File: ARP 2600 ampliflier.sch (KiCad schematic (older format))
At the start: 39 parts, among them P1 CONN_01X04, P2 CONN_01X04, P3 CONN_01X04, P4 CONN_01X04, Q1 PN2222A, U1 TDA7269A, U2 LM7812CT, U3 LM7912CT

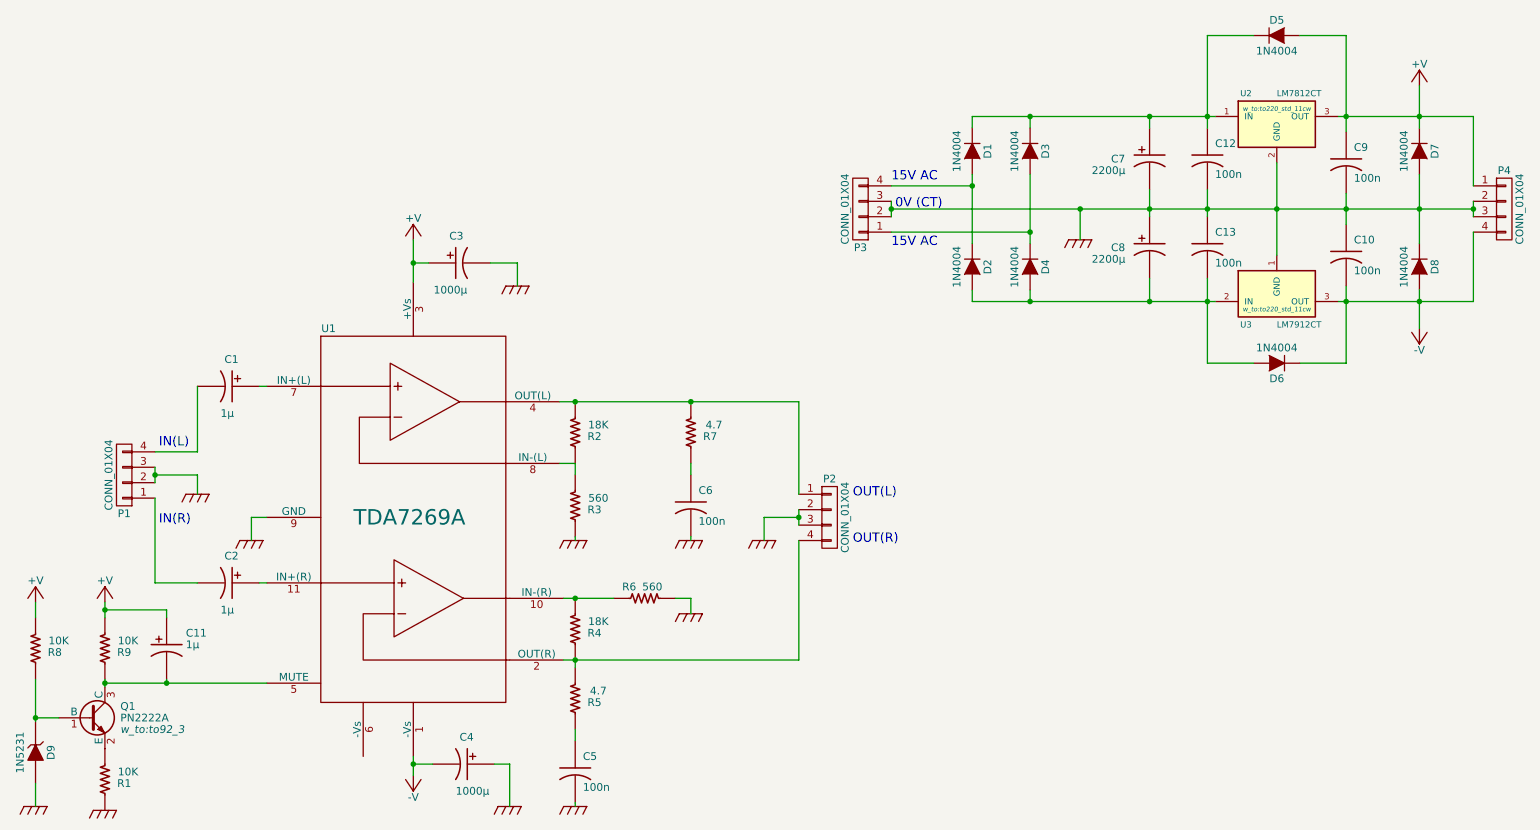
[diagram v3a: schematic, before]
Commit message: fixed pintout error with T0-220 footprints, fix Q1 footprint pintout error, add keepout zones to heatsink landing areas on top copper
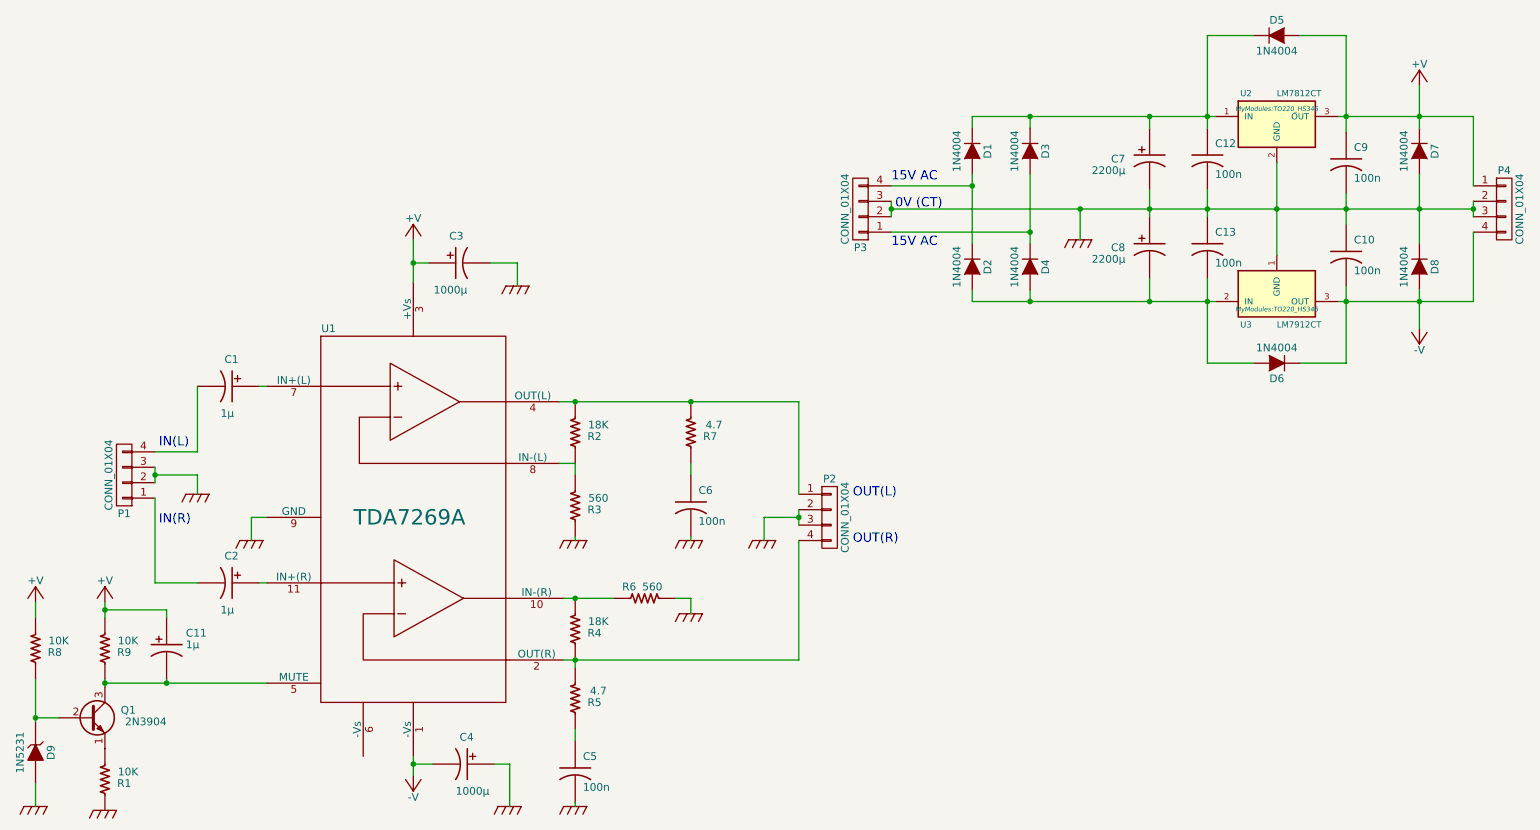
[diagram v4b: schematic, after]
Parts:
- removed Q1: PN2222A, w_to:to92_3, symbol PN2222A
- added Q1: 2N3904, symbol Q_NPN_EBC
- U2, U3: footprint w_to:to220_std_11cw -> MyModules:TO220_HS346
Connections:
- net at C11.2 (-), R9.2, U1.5 (MUTE): now also Q1.3 (C)
- net at R1.1: now also Q1.1 (E)
- net at D9.1 (K), R8.2: now also Q1.2 (B)
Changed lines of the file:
@@
 F 0 "U2" H 8950 2325 40  0000 C CNN
 F 1 "LM7812CT" H 9150 2325 40  0000 L CNN
-F 2 "w_to:to220_std_11cw" H 9150 2225 30  0000 C CIN
+F 2 "MyModules:TO220_HS346" H 9150 2225 30  0000 C CIN
 F 3 "" H 9150 2125 60  0000 C CNN
 	1    9150 2125
@@
 F 0 "U3" H 8950 3025 40  0000 C CNN
 F 1 "LM7912CT" H 9150 3025 40  0000 L CNN
-F 2 "w_to:to220_std_11cw" H 9150 3125 30  0000 C CIN
+F 2 "MyModules:TO220_HS346" H 9150 3125 30  0000 C CIN
 F 3 "" H 9150 3225 60  0000 C CNN
 	1    9150 3225
@@
 0V (CT)
 $Comp
-L PN2222A Q1
-U 1 1 5855A305
-P 1450 5975
-F 0 "Q1" H 1650 6050 50  0000 L CNN
-F 1 "PN2222A" H 1650 5975 50  0000 L CNN
-F 2 "w_to:to92_3" H 1650 5900 50  0000 L CIN
-F 3 "" H 1450 5975 50  0000 L CNN
-	1    1450 5975
-	1    0    0    -1
-$EndComp
-$Comp
 L ZENER D9
 U 1 1 5855AB7A
@@
 	8700 2550 8700 2725
 Connection ~ 8700 2675
+$Comp
+L Q_NPN_EBC Q1
+U 1 1 58684547
+P 1450 5975
+F 0 "Q1" H 1750 6025 50  0000 R CNN
+F 1 "2N3904" H 1950 5950 50  0000 R CNN
+F 2 "" H 1650 6075 29  0000 C CNN
+F 3 "" H 1450 5975 60  0000 C CNN
+	1    1450 5975
+	1    0    0    -1
+$EndComp
 $EndSCHEMATC

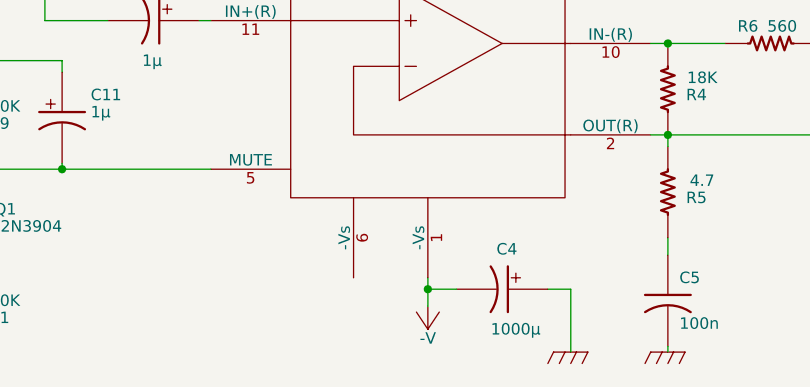
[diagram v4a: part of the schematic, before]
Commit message: fixed another mistake - two -Vs pins on amplifier you donut
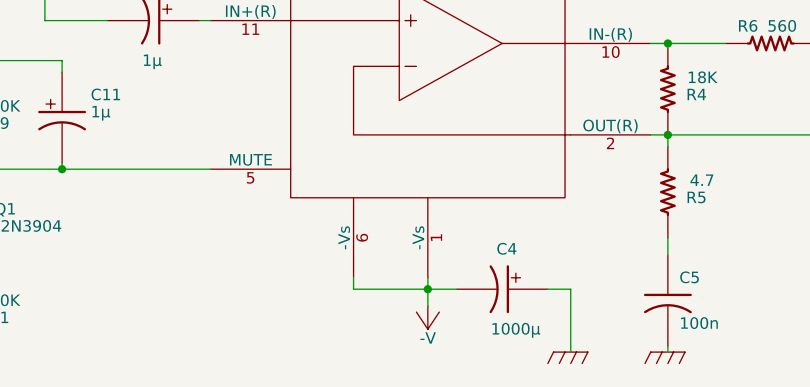
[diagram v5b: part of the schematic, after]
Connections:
- net -V: now also U1.6 (-Vs)
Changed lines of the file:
@@
 	3550 6225 3550 6350
 Wire Wire Line
-	3675 6275 3550 6275
+	3225 6275 3675 6275
 Connection ~ 3550 6275
 $Comp
@@
 	1    0    0    -1
 $EndComp
+Wire Wire Line
+	3225 6225 3225 6275
 $EndSCHEMATC
